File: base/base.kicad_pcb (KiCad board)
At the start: 4 copper layers, 30 x 90 mm, 6 parts, among them J1 DF40TC(4.0)-30DS-0.4V(51), J2 DIP-48_SocketStrip_SMD

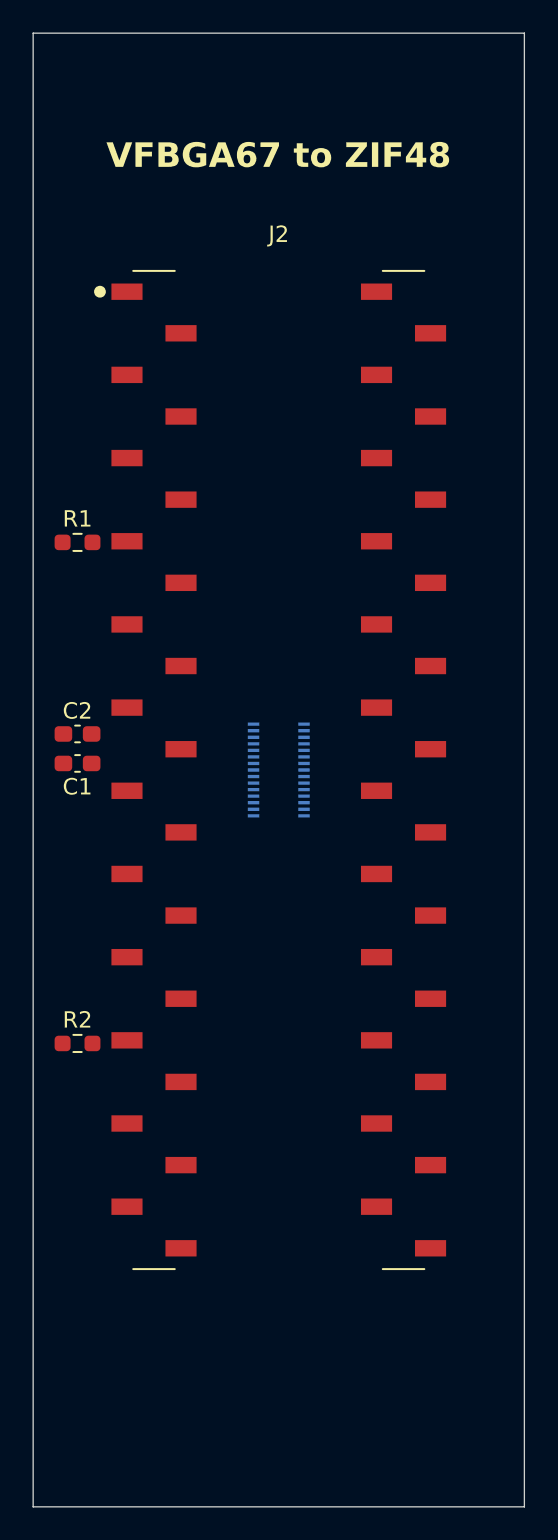
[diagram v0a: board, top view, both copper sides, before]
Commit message: Commit routed pinout, checkers, docs and mechanical outputs
Brings the repository up to the state that has been on disk and passing
`make check`: the routed same-number DF40 table replacing the old Courk
DF17-derived pinout, the mating and panel checkers, corrected connector
documentation, JLC rule tooling, and the 3D/mechanical outputs.

Committed as one baseline so the board C and board D work that follows has
reviewable per-task diffs.

Co-Authored-By: Claude Opus 5 <noreply@anthropic.com>
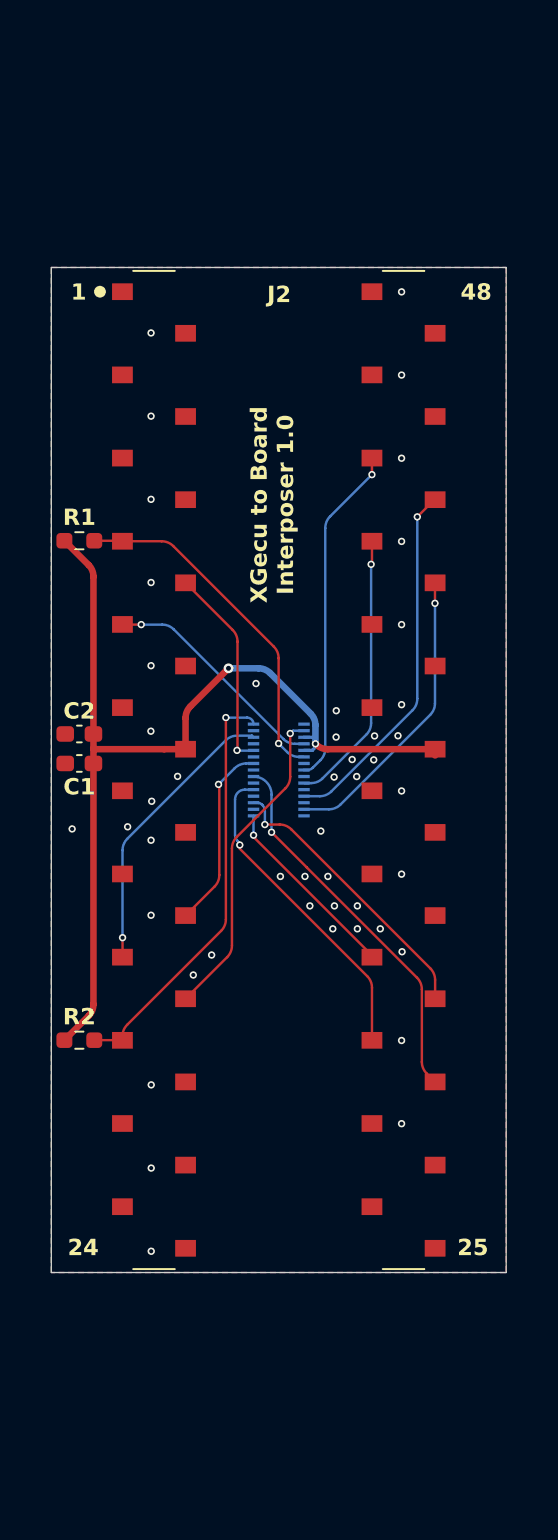
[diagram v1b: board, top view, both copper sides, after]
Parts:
- J2: value DIP-48_SocketStrip_SMD -> DIP-48_Socket
- moved R2 0.23 mm to (111.9, 107.7)
- moved R1 0.15 mm to (111.9, 77.2)
- moved C1 0.11 mm to (111.9, 90.8)
- moved C2 0.11 mm to (111.9, 89.0)
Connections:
- J1 pad 1: GND -> //WP
- J1 pad 10: //WP -> VCC
- J1 pad 11: //CE -> GND
- J1 pad 12: //RE -> /RY//BY
- J1 pad 14: VCC -> GND
- J1 pad 16: GND -> /IO8
- J1 pad 17: GND -> /IO1
- J1 pad 18: /IO5 -> GND
- J1 pad 20: /IO2 -> /IO6
- J1 pad 21: /IO6 -> /IO2
- J1 pad 22: /IO1 -> GND
- J1 pad 23: /IO8 -> GND
- J1 pad 24: /IO3 -> /IO7
- J1 pad 25: /IO7 -> /IO3
- J1 pad 26: /IO4 -> GND
- J1 pad 28: GND -> /IO5
- J1 pad 29: GND -> /IO4
- J1 pad 4: GND -> //WE
- J1 pad 5: GND -> /ALE
- J1 pad 6: GND -> VCC
- J1 pad 7: /RY//BY -> GND
- J1 pad 8: /ALE -> //CE
- J1 pad 9: //WE -> //RE
- J2 pad 1: unconnected-(J2-NC-Pad1) -> GND
- J2 pad 10: unconnected-(J2-NC-Pad10) -> GND
- J2 pad 11: unconnected-(J2-NC-Pad11) -> GND
- J2 pad 15: unconnected-(J2-NC-Pad15) -> GND
- J2 pad 20: unconnected-(J2-NC-Pad20) -> GND
- J2 pad 28: unconnected-(J2-NC-Pad28) -> GND
- J2 pad 33: unconnected-(J2-NC-Pad33) -> GND
- J2 pad 38: unconnected-(J2-NC-Pad38) -> GND
- J2 pad 40: unconnected-(J2-NC-Pad40) -> GND
- J2 pad 45: unconnected-(J2-NC-Pad45) -> GND
- J2 pad 48: unconnected-(J2-NC-Pad48) -> GND
- J2 pad 6: unconnected-(J2-NC-Pad6) -> GND
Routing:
- net VCC: track 0.00 -> 61.3 mm, vias 0 -> 2
- net //WP: track 0.00 -> 25.9 mm, vias 0 -> 1
- net /IO1: track 0.00 -> 23.5 mm, vias 0 -> 1
- net /IO7: track 0.00 -> 22.2 mm, vias 0 -> 1
- net /RY//BY: track 0.00 -> 21.4 mm, vias 0 -> 1
- net /IO8: track 0.00 -> 20.9 mm, vias 0 -> 1
- net //WE: track 0.00 -> 19.6 mm, vias 0 -> 1
- net /IO2: track 0.00 -> 19.6 mm, vias 0 -> 1
- net /IO5: track 0.00 -> 18.2 mm, vias 0 -> 1
- net /ALE: track 0.00 -> 17.6 mm, vias 0 -> 1
- net /IO3: track 0.00 -> 17.4 mm, vias 0 -> 1
- net /IO6: track 0.00 -> 16.9 mm, vias 0 -> 1
- net //CE: track 0.00 -> 14.0 mm, vias 0 -> 1
- net //RE: track 0.00 -> 12.3 mm, vias 0 -> 1
- net /IO4: track 0.00 -> 11.6 mm, vias 0 -> 1
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- added copper zone on B.Cu, net GND
- added copper zone on F.Cu, net GND
- added copper zone on In1.Cu, net GND
- added copper zone on In2.Cu, net GND
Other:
- board size 30 x 90 mm -> 27.8 x 61.4 mm
- board text added: "1"
- board text added: "23 IO1 30 IO2 31 IO3 32 IO4 37 VCC 41 IO5 42 IO6 43 IO7 44 IO8"
- board text added: "24"
- board text added: "25"
- board text added: "4 /WE 6 VCC 8 /CE 10 VCC 12 RY//BY 16 IO8 20 IO6 24 IO7 28 IO5"
- board text added: "48"
- board text added: "DF40TC: 1 /WP 5 ALE 9 /RE 13 CLE 17 IO1 21 IO2 25 IO3 29 IO4"
- board text added: "DIP48: 7 RY//BY 8 /RE 9 /CE 12 VCC 16 CLE 17 ALE 19 /WE 19 /WP"
- board text added: "Rev A A. Gompper"
- board text added: "XGecu to Board Interposer 1.0"
- board text removed: "VFBGA67 to ZIF48"
